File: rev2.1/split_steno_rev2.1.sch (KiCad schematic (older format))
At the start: 64 parts, among them J1 USB_OTG, J2 Audio-Jack-4, P1 TC2030-IDC, SW1 SW_Push, SW10 SW_Push, SW11 SW_Push, SW12 SW_Push, SW13 SW_Push, SW14 SW_Push, SW15 SW_Push, SW16 SW_Push, SW17 SW_Push, SW18 SW_Push, SW19 SW_Push, SW2 SW_Push, SW20 SW_Push, SW21 SW_Push, SW22 Switch-6P-2S2T, SW3 SW_Push, SW4 SW_Push, SW5 SW_Push, SW6 SW_Push, SW7 SW_Push, SW8 SW_Push, SW9 SW_Push, U1 74LVC1G34, U2 MCP73831, U3 MCP1700, U4 MCP1700, U5 ATXMEGA128A4U-AU, U6 nRF24L01_module

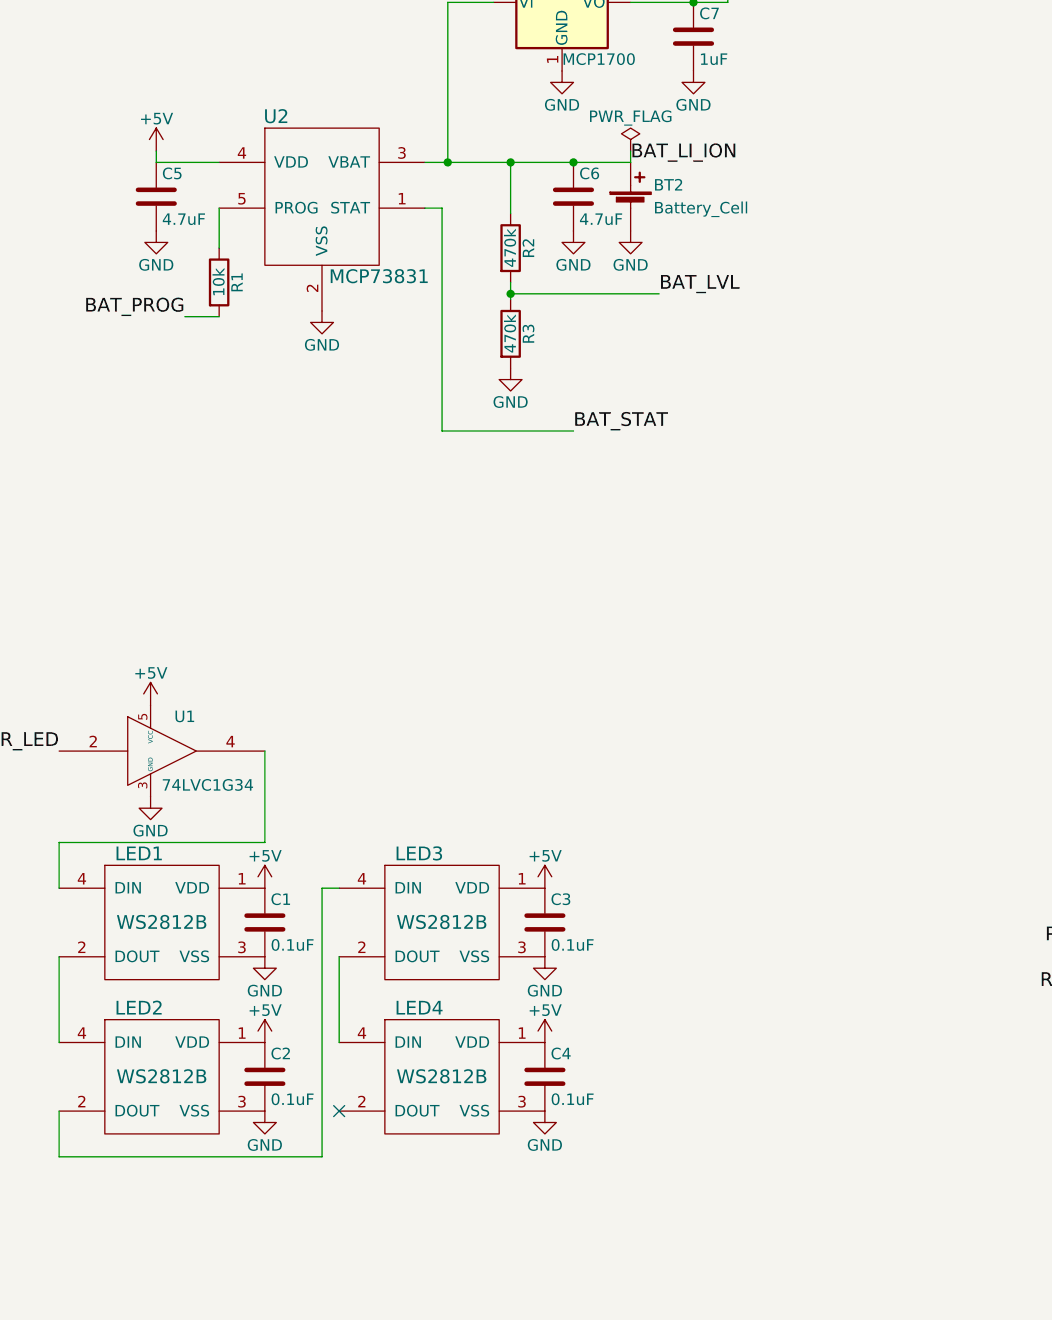
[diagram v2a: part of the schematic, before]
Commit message: added 2 more ws2812b
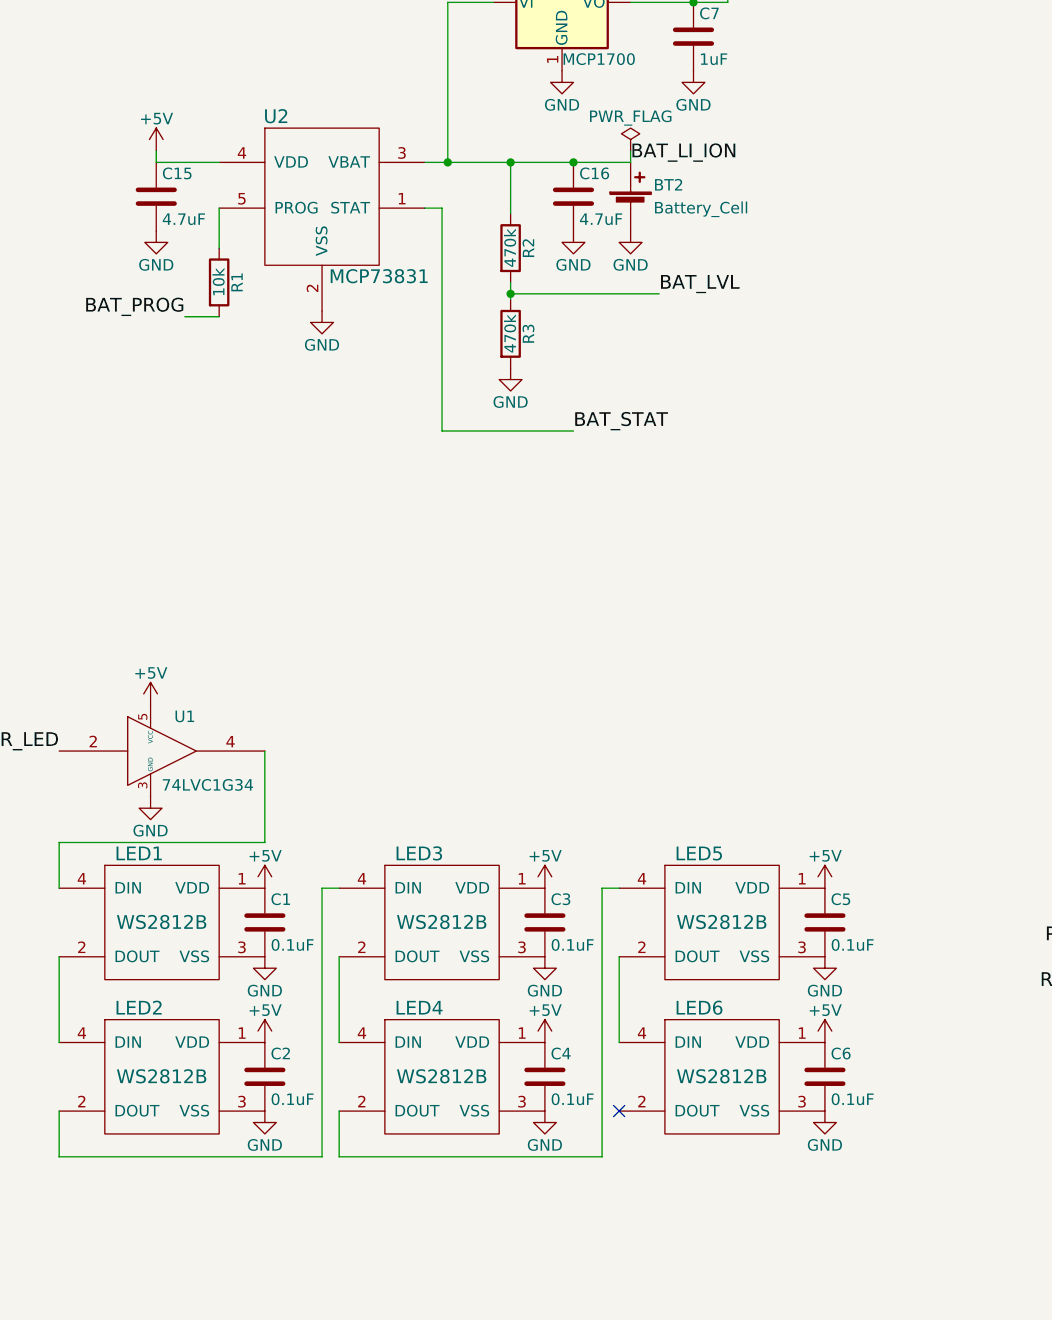
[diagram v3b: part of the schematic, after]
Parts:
- added C5, C6: 0.1uF, Capacitors_SMD:C_0603_HandSoldering, symbol C
- added LED5, LED6: WS2812B, WS2812B:WS2812B, symbol WS2812B
- renumbered C5 to C15, C6 to C16
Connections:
- net +5V: now also C5.1, C6.1, LED5.1 (VDD), LED6.1 (VDD)
- net GND: now also C5.2, C6.2, LED5.3 (VSS), LED6.3 (VSS)
- net at LED4.2 (DOUT): now also LED5.4 (DIN)
- new net: LED5.2 (DOUT), LED6.4 (DIN)
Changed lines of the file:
@@
 	1    0    0    -1
 $EndComp
-NoConn ~ 3050 7150
 $Comp
 L 74LVC1G34 U1
@@
 $EndComp
 $Comp
-L C C5
+L C C15
 U 1 1 5AB52BE0
 P 2250 3150
-F 0 "C5" H 2275 3250 50  0000 L CNN
+F 0 "C15" H 2275 3250 50  0000 L CNN
 F 1 "4.7uF" H 2275 3050 50  0000 L CNN
 F 2 "Capacitors_SMD:C_0603_HandSoldering" H 2288 3000 50  0001 C CNN
@@
 $EndComp
 $Comp
-L C C6
+L C C16
 U 1 1 5AB52D41
 P 4075 3150
-F 0 "C6" H 4100 3250 50  0000 L CNN
+F 0 "C16" H 4100 3250 50  0000 L CNN
 F 1 "4.7uF" H 4100 3050 50  0000 L CNN
 F 2 "Capacitors_SMD:C_0603_HandSoldering" H 4113 3000 50  0001 C CNN
@@
 VBUS_CHECK
 NoConn ~ 14175 7100
+$Comp
+L WS2812B LED6
+U 1 1 5AC843BB
+P 4725 7000
+F 0 "LED6" H 4625 7300 60  0000 C CNN
+F 1 "WS2812B" H 4725 7000 60  0000 C CNN
+F 2 "WS2812B:WS2812B" H 4725 7000 60  0001 C CNN
+F 3 "" H 4725 7000 60  0001 C CNN
+	1    4725 7000
+	1    0    0    -1
+$EndComp
+$Comp
+L +5V #PWR054
+U 1 1 5AC843C2
+P 5175 6175
+F 0 "#PWR054" H 5175 6025 50  0001 C CNN
+F 1 "+5V" H 5175 6315 50  0000 C CNN
+F 2 "" H 5175 6175 50  0001 C CNN
+F 3 "" H 5175 6175 50  0001 C CNN
+	1    5175 6175
+	1    0    0    -1
+$EndComp
+$Comp
+L +5V #PWR055
+U 1 1 5AC843C8
+P 5175 6850
+F 0 "#PWR055" H 5175 6700 50  0001 C CNN
+F 1 "+5V" H 5175 6990 50  0000 C CNN
+F 2 "" H 5175 6850 50  0001 C CNN
+F 3 "" H 5175 6850 50  0001 C CNN
+	1    5175 6850
+	1    0    0    -1
+$EndComp
+$Comp
+L GND #PWR056
+U 1 1 5AC843CE
+P 5175 6475
+F 0 "#PWR056" H 5175 6225 50  0001 C CNN
+F 1 "GND" H 5175 6325 50  0000 C CNN
+F 2 "" H 5175 6475 50  0001 C CNN
+F 3 "" H 5175 6475 50  0001 C CNN
+	1    5175 6475
+	1    0    0    -1
+$EndComp
+$Comp
+L GND #PWR057
+U 1 1 5AC843D4
+P 5175 7150
+F 0 "#PWR057" H 5175 6900 50  0001 C CNN
+F 1 "GND" H 5175 7000 50  0000 C CNN
+F 2 "" H 5175 7150 50  0001 C CNN
+F 3 "" H 5175 7150 50  0001 C CNN
+	1    5175 7150
+	1    0    0    -1
+$EndComp
+NoConn ~ 4275 7150
+$Comp
+L WS2812B LED5
+U 1 1 5AC843DB
+P 4725 6325
+F 0 "LED5" H 4625 6625 60  0000 C CNN
+F 1 "WS2812B" H 4725 6325 60  0000 C CNN
+F 2 "WS2812B:WS2812B" H 4725 6325 60  0001 C CNN
+F 3 "" H 4725 6325 60  0001 C CNN
+	1    4725 6325
+	1    0    0    -1
+$EndComp
+$Comp
+L C C5
+U 1 1 5AC843E2
+P 5175 6325
+F 0 "C5" H 5200 6425 50  0000 L CNN
+F 1 "0.1uF" H 5200 6225 50  0000 L CNN
+F 2 "Capacitors_SMD:C_0603_HandSoldering" H 5213 6175 50  0001 C CNN
+F 3 "" H 5175 6325 50  0001 C CNN
+	1    5175 6325
+	1    0    0    -1
+$EndComp
+$Comp
+L C C6
+U 1 1 5AC843E9
+P 5175 7000
+F 0 "C6" H 5200 7100 50  0000 L CNN
+F 1 "0.1uF" H 5200 6900 50  0000 L CNN
+F 2 "Capacitors_SMD:C_0603_HandSoldering" H 5213 6850 50  0001 C CNN
+F 3 "" H 5175 7000 50  0001 C CNN
+	1    5175 7000
+	1    0    0    -1
+$EndComp
+Wire Wire Line
+	4200 6175 4275 6175
+Wire Wire Line
+	4275 6850 4275 6475
+Wire Wire Line
+	4200 6175 4200 7350
+Wire Wire Line
+	4200 7350 3050 7350
+Wire Wire Line
+	3050 7350 3050 7150
 $EndSCHEMATC

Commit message: finished mounting hole placement
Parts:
- SW21: footprint switch:SwitchPush_C&K_MultiFoot_RS-187R05A2-DS_And_PTS645_SMT -> Keebio-Parts:SW_Tactile_SPST_Angled_MJTP1117
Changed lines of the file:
@@
 F 0 "SW21" H 8475 5000 50  0000 L CNN
 F 1 "SW_Push" H 8425 4840 50  0000 C CNN
-F 2 "switch:SwitchPush_C&K_MultiFoot_RS-187R05A2-DS_And_PTS645_SMT" H 8425 5100 50  0001 C CNN
+F 2 "Keebio-Parts:SW_Tactile_SPST_Angled_MJTP1117" H 8425 5100 50  0001 C CNN
 F 3 "" H 8425 5100 50  0001 C CNN
 	1    8425 4900

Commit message: updated some footprints
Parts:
- BT1: footprint Battery_Holders:Keystone_1058_1x2032-CoinCell -> battery:CR2032_BK-913
- JP1, JP2, JP3: footprint keyboard_parts:SOLDER_JUMPER_2 -> jumper:Jumper_1x02_P2.54mm_THT
- P1: footprint Connectors:Tag-Connect_TC2030-IDC-NL -> Tag-Connect:TC2030-NL_SMALL_AND_IDC_PDI_Extra_Pads
- SW15, SW16, SW5, SW6: footprint Keebio-Parts:Hybrid_PCB_100H_Dual_hole -> Keebio-Parts:Hybrid_PCB_100H_Dual_hole-flip
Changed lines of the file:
@@
 F 0 "BT1" H 2600 1750 50  0000 L CNN
 F 1 "Battery" H 2600 1650 50  0000 L CNN
-F 2 "Battery_Holders:Keystone_1058_1x2032-CoinCell" V 2500 1710 50  0001 C CNN
+F 2 "battery:CR2032_BK-913" V 2500 1710 50  0001 C CNN
 F 3 "" V 2500 1710 50  0001 C CNN
 	1    2500 1650
@@
 F 0 "JP1" H 3225 1975 50  0000 C CNN
 F 1 "Jumper" H 3225 1745 50  0000 C CNN
-F 2 "keyboard_parts:SOLDER_JUMPER_2" H 3225 1825 50  0001 C CNN
+F 2 "jumper:Jumper_1x02_P2.54mm_THT" H 3225 1825 50  0001 C CNN
 F 3 "" H 3225 1825 50  0001 C CNN
 	1    3225 1825
@@
 F 0 "JP2" H 5425 2300 50  0000 C CNN
 F 1 "Jumper" H 5425 2070 50  0000 C CNN
-F 2 "keyboard_parts:SOLDER_JUMPER_2" H 5425 2150 50  0001 C CNN
+F 2 "jumper:Jumper_1x02_P2.54mm_THT" H 5425 2150 50  0001 C CNN
 F 3 "" H 5425 2150 50  0001 C CNN
 	1    5425 2150
@@
 F 0 "JP3" H 6900 1400 50  0000 C CNN
 F 1 "Jumper" H 6900 1170 50  0000 C CNN
-F 2 "keyboard_parts:SOLDER_JUMPER_2" H 6900 1250 50  0001 C CNN
+F 2 "jumper:Jumper_1x02_P2.54mm_THT" H 6900 1250 50  0001 C CNN
 F 3 "" H 6900 1250 50  0001 C CNN
 	1    6900 1250
@@
 F 0 "P1" H 6475 6325 40  0000 L CNN
 F 1 "TC2030-IDC" H 6525 6725 40  0000 C CNN
-F 2 "Connectors:Tag-Connect_TC2030-IDC-NL" H 6525 6525 60  0001 C CNN
+F 2 "Tag-Connect:TC2030-NL_SMALL_AND_IDC_PDI_Extra_Pads" H 6525 6525 60  0001 C CNN
 F 3 "" H 6525 6525 60  0001 C CNN
 	1    6525 6525
@@
 F 0 "SW5" H 3075 9100 50  0000 L CNN
 F 1 "SW_Push" H 3025 8940 50  0000 C CNN
-F 2 "Keebio-Parts:Hybrid_PCB_100H_Dual_hole" H 3025 9200 50  0001 C CNN
+F 2 "Keebio-Parts:Hybrid_PCB_100H_Dual_hole-flip" H 3025 9200 50  0001 C CNN
 F 3 "" H 3025 9200 50  0001 C CNN
 	1    3025 9000
@@
 F 0 "SW6" H 3075 9350 50  0000 L CNN
 F 1 "SW_Push" H 3025 9190 50  0000 C CNN
-F 2 "Keebio-Parts:Hybrid_PCB_100H_Dual_hole" H 3025 9450 50  0001 C CNN
+F 2 "Keebio-Parts:Hybrid_PCB_100H_Dual_hole-flip" H 3025 9450 50  0001 C CNN
 F 3 "" H 3025 9450 50  0001 C CNN
 	1    3025 9250
@@
 F 0 "SW15" H 4525 9600 50  0000 L CNN
 F 1 "SW_Push" H 4475 9440 50  0000 C CNN
-F 2 "Keebio-Parts:Hybrid_PCB_100H_Dual_hole" H 4475 9700 50  0001 C CNN
+F 2 "Keebio-Parts:Hybrid_PCB_100H_Dual_hole-flip" H 4475 9700 50  0001 C CNN
 F 3 "" H 4475 9700 50  0001 C CNN
 	1    4475 9500
@@
 F 0 "SW16" H 4525 9850 50  0000 L CNN
 F 1 "SW_Push" H 4475 9690 50  0000 C CNN
-F 2 "Keebio-Parts:Hybrid_PCB_100H_Dual_hole" H 4475 9950 50  0001 C CNN
+F 2 "Keebio-Parts:Hybrid_PCB_100H_Dual_hole-flip" H 4475 9950 50  0001 C CNN
 F 3 "" H 4475 9950 50  0001 C CNN
 	1    4475 9750

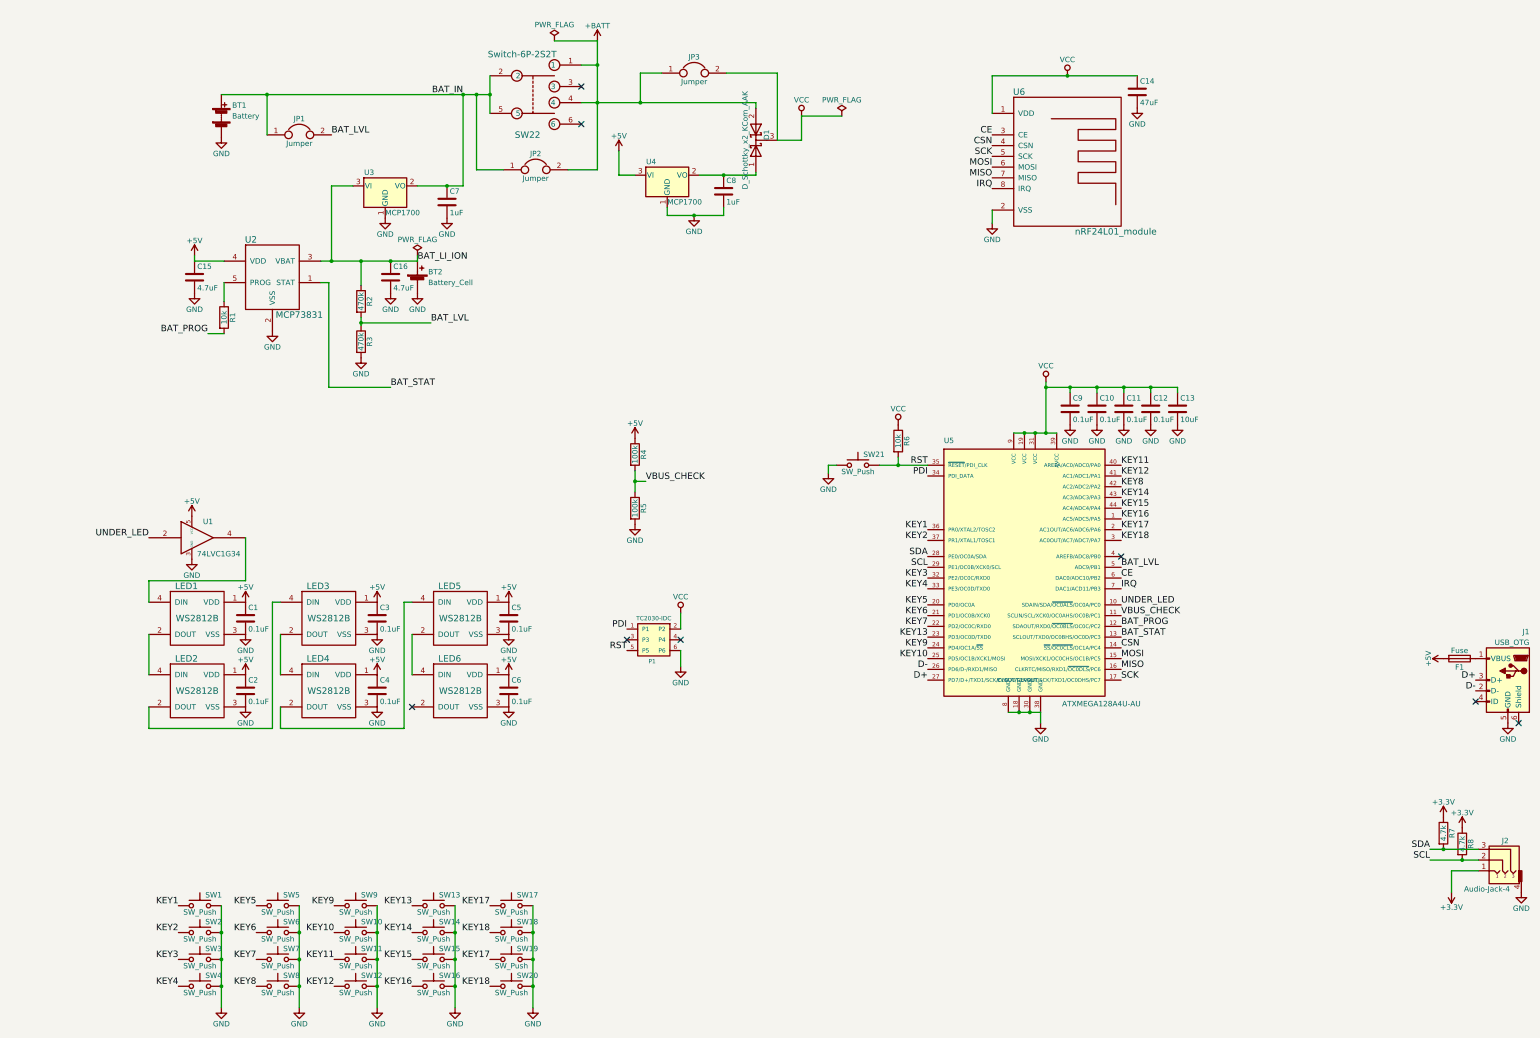
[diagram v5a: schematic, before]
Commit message: removed lipo charging circuit
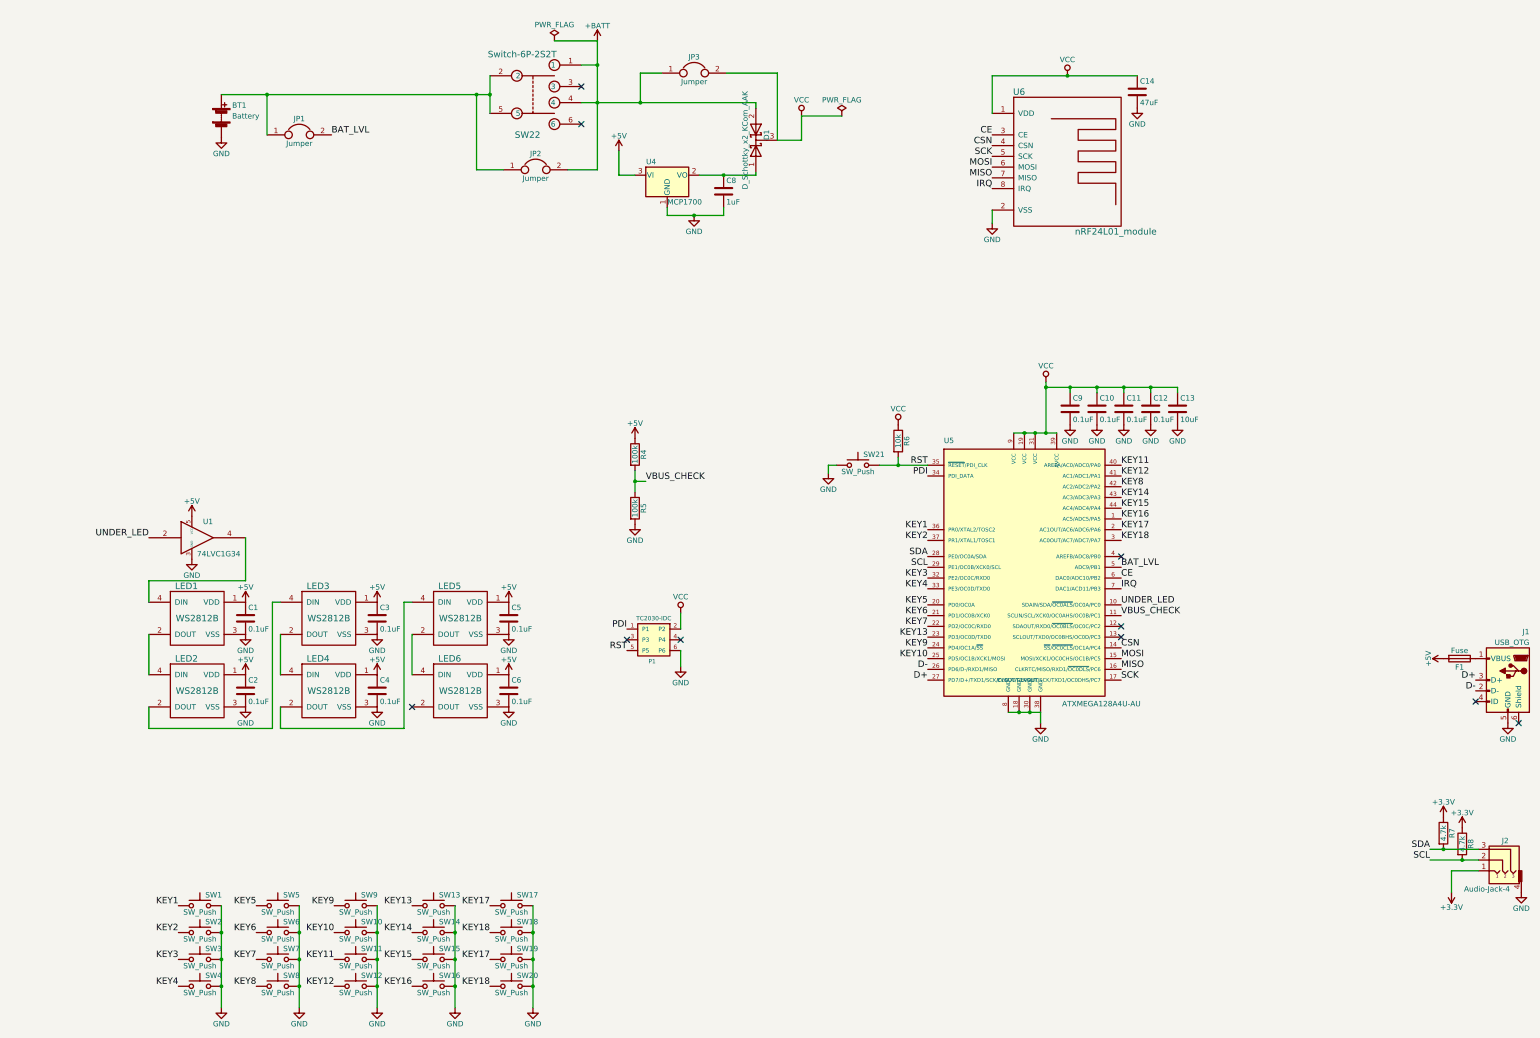
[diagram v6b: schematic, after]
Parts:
- removed BT2: Battery_Cell, Connectors_JST:JST_PH_S2B-PH-K_02x2.00mm_Angled, symbol Battery_Cell
- removed C15, C16: 4.7uF, Capacitors_SMD:C_0603_HandSoldering, symbol C
- removed C7: 1uF, Capacitors_SMD:C_0603_HandSoldering, symbol C
- removed R1: 10k, Resistors_SMD:R_0603_HandSoldering, symbol R
- removed R2, R3: 470k, Resistors_SMD:R_0603_HandSoldering, symbol R
- removed U2: MCP73831, TO_SOT_Packages_SMD:SOT-23-5_HandSoldering, symbol MCP73831
- removed U3: MCP1700, TO_SOT_Packages_SMD:SOT-23, symbol MCP1700
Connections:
- net BAT_IN: no longer names the net of BT1.1 (+), JP1.1, JP2.1, SW22.2, SW22.5
- net BAT_PROG: no longer names the net of U5.12 (SDAOUT/RXD0/~OC0BLS~/OC0C/PC2)
- net BAT_STAT: no longer names the net of U5.13 (SCLOUT/TXD0/OC0BHS/OC0D/PC3)
- no-connect marks 8 -> 10
